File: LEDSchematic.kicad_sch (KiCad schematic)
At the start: 2 parts

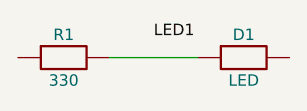
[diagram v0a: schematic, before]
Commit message: feat(schematic): MVP .kicad_sch serializer + symbol/wire/label tools
- Drawable schematic model (Schematic/SchSymbol/Wire/NetLabel)
- Embedded symbol library with generic 2-pin fallback
- schematic_create/symbol_add/wire_add/label_add/schematic_info/schematic_export_sch
- README (pt-BR + EN) + CHANGELOG; test count 189
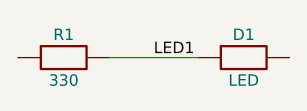
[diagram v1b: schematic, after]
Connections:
- net LED1: now also D1.1, R1.2
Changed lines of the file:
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@@
     (stroke (width 0) (type default))
   )
-  (label "LED1" (at 110 78 0)
+  (label "LED1" (at 110 80 0)
     (effects (font (size 1.27 1.27)) (justify left bottom))
   )
@@
     (instances
       (project "LEDSchematic"
-        (path "/ac408772-1d9b-4cbc-8ff3-19bb1d213516" (reference "R1") (unit 1))
+        (path "/fc0a31aa-4f3e-4efd-b31a-801c10b1087b" (reference "R1") (unit 1))
       )
     )
@@
     (instances
       (project "LEDSchematic"
-        (path "/457fea11-d5b6-4ef0-b573-9aa1083dbe93" (reference "D1") (unit 1))
+        (path "/632c2709-09bb-43a5-ba8c-7fd1eb77ecab" (reference "D1") (unit 1))
       )
     )
